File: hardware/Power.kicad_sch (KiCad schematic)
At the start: 28 parts, among them Q1 SiS415DNT, U4 SiA462DJ

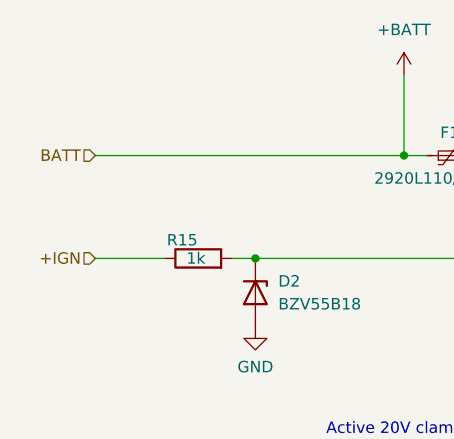
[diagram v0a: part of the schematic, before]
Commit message: PCB Basic outline
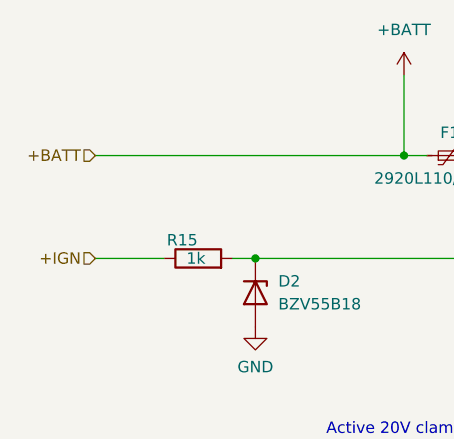
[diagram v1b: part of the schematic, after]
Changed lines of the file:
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@@
 		)
 	)
-	(hierarchical_label "BATT"
+	(hierarchical_label "+BATT"
 		(shape input)
 		(at 33.02 96.52 180)
@@
 		(length 2.54)
 		(shape round)
-		(at 55.88 96.52 0)
+		(at 48.26 96.52 0)
 		(fields_autoplaced yes)
 		(effects
@@
 			(justify left bottom)
 		)
-		(property "Netclass" "Batt"
-			(at 56.5785 93.98 0)
+		(property "Netclass" "High Current"
+			(at 48.9585 93.98 0)
 			(effects
 				(font

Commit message: Pre DRC, almost done!
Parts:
- removed C6: EMK325ABJ107MM-T, Capacitor_SMD:C_1210_3225Metric_Pad1.33x2.70mm_HandSolder, symbol Device:C
- removed D3: B360, Diode_SMD:D_SMC, symbol Diode:B360
- removed L2: 100uH, Inductor_SMD:L_Bourns_SRR1260, symbol Device:L
- removed PS1: LM2576HVS-5, Package_TO_SOT_SMD:TO-263-5_TabPin3, symbol Regulator_Switching:LM2576HVS-5
- removed Q1: SiS415DNT, Package_SO:Vishay_PowerPAK_1212-8_Single, symbol Transistor_FET:SiS415DNT
- removed R1: 2.2k, Resistor_SMD:R_1206_3216Metric_Pad1.30x1.75mm_HandSolder, symbol Device:R
- removed R16: 100k, Resistor_SMD:R_1206_3216Metric_Pad1.30x1.75mm_HandSolder, symbol Device:R
- removed TP11: GND, TestPoint:TestPoint_Pad_D1.5mm, symbol Connector:TestPoint
- removed U4: SiA462DJ, Package_TO_SOT_SMD:Vishay_PowerPAK_SC70-6L_Single, symbol Transistor_FET:SiA462DJ
- added PS1: LMZM23600V5, Package_LGA:Texas_SIL0010A_MicroSiP-10-1EP_3.8x3mm_P0.6mm_EP0.7x2.9mm_ThermalVias, symbol Regulator_Switching:LMZM23600V5
- added TP9: GND, TestPoint:TestPoint_THTPad_D2.0mm_Drill1.0mm, symbol Connector:TestPoint
- L1: value 100uH -> 330uH; footprint Inductor_SMD:L_Bourns_SRR1260 -> myESP32s:L_Bourns_SRR7045; MPN SRR1260-101M -> SRR7045-331M
- TP10: footprint TestPoint:TestPoint_Pad_D1.5mm -> TestPoint:TestPoint_THTPad_D2.0mm_Drill1.0mm
- TP2: footprint TestPoint:TestPoint_Pad_D1.5mm -> TestPoint:TestPoint_THTPad_D1.0mm_Drill0.5mm
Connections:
- net GND: now also D1.2 (A), R2.2, PS1.1 (GND), PS1.11 (GND), PS1.2 (MODE/SYNC), TP9.1
- net at R2.1: now also C13.1, D2.1 (K), R15.2, TP2.1, PS1.4 (EN)
- net at C2.1, C3.1, C4.1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: now also PS1.3 (VIN); no longer R2.2
- net at C5.1, R17.1: now also PS1.6 (VOUT), PS1.7 (FB)
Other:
- note removed: "Active 20V clamp"
- moved on the sheet: F1, R2, TP1

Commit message: Improving documentation
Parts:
- TP10, TP9: now left out of the parts list
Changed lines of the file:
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@@
 		(unit 1)
 		(exclude_from_sim no)
-		(in_bom yes)
+		(in_bom no)
 		(on_board yes)
 		(dnp no)
@@
 		(unit 1)
 		(exclude_from_sim no)
-		(in_bom yes)
-		(on_board yes)
-		(dnp no)
+		(in_bom no)
+		(on_board yes)
+		(dnp no)
